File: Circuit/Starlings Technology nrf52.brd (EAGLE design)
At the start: 53.3 x 52.7 mm, 54 parts, among them IC1 MCP1703CB, J4 USB Micro, J7 CORTEX_DEBUG_SMD, Q2 BSS84, SW1 FSM8JSMASTR, SW2 FSM8JSMASTR, U1 TPS61259YFFR, U2 MCP73831, U3 BC840M, U5 74AHCT2G125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

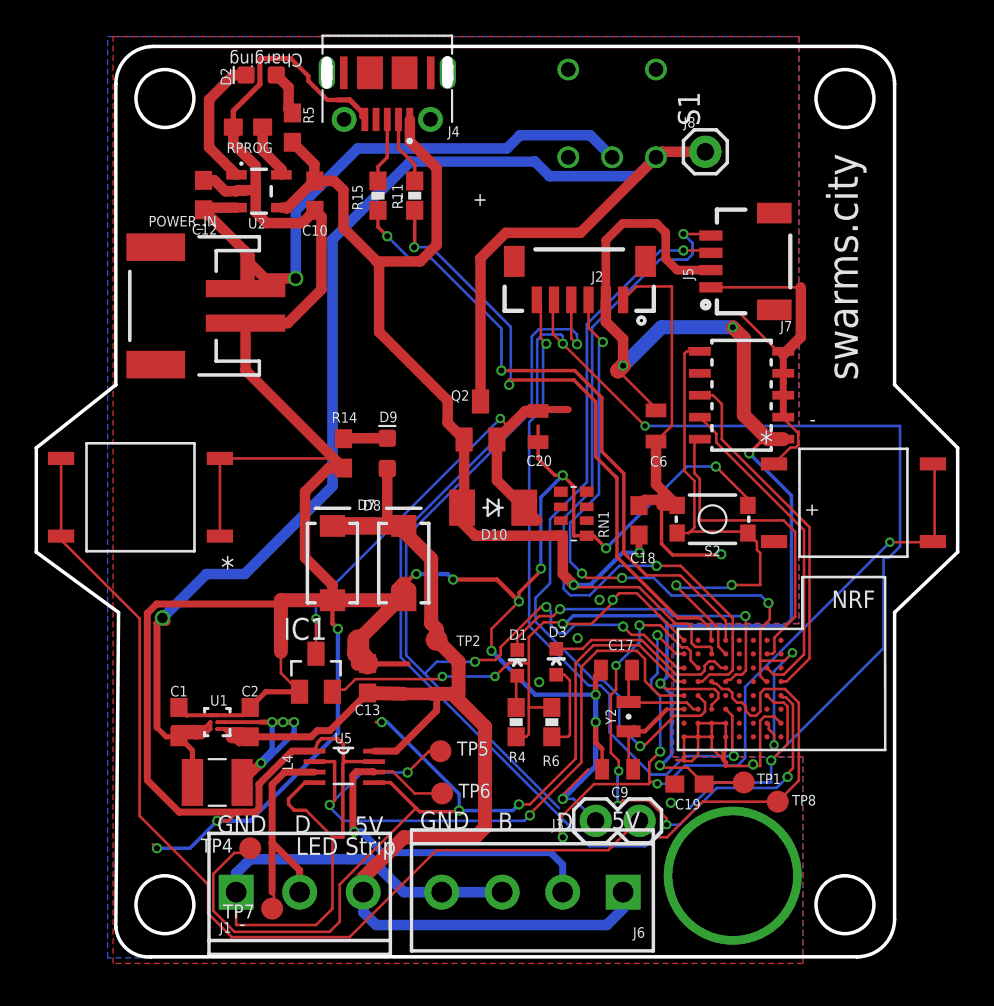
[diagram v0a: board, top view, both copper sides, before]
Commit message: Switching 3.5mm terminal blocks to 2.54mm (0.1") pitch header pins for painless led attachment. Also making buttons perfectly symmetric.
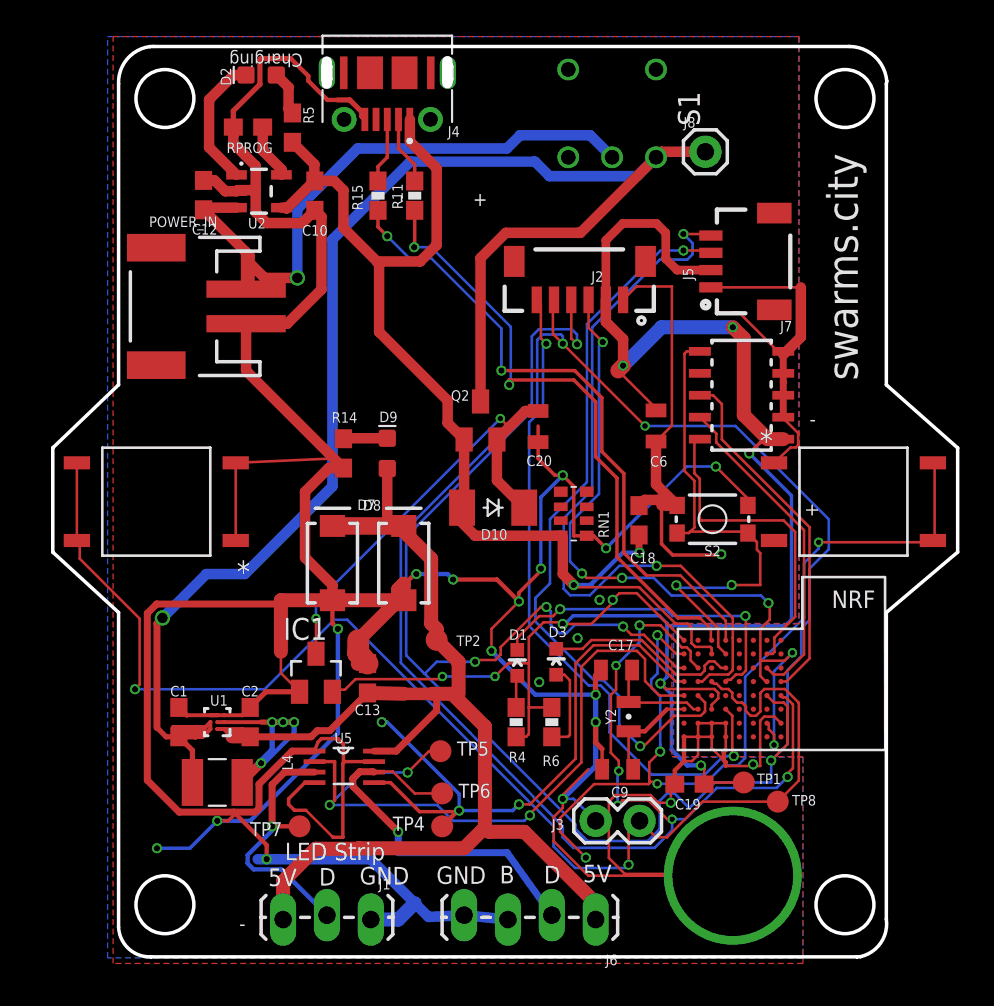
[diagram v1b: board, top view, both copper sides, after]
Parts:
- J1: device SparkFun-Connectors:SCREWTERMINAL-3.5MM-3_LOCK.007S -> SparkFun-Connectors:1X03_LOCK_LONGPADS
- J6: device SparkFun-Connectors:SCREWTERMINAL-3.5MM-4 -> SparkFun-Connectors:1X04_LOCK_LONGPADS
- moved TP4 11.2 mm to (14.9, 7.94)
- moved J1 7.78 mm to (10.8, 2.54), turned to 180 degrees
- moved TP7 5.02 mm to (6.67, 7.94)
- moved J6 2.25 mm to (23.8, 2.54)
- moved SW1 0.95 mm to (-1.63, 26.7)
- moved SW2 0.06 mm to (38.7, 26.7)
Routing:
- net HEADLAMP_3V3: track 56.5 -> 35.3 mm
- net GND: track 333.3 -> 352.4 mm, vias 21 -> 22
- net SWITCH_2: track 47.6 -> 51.8 mm
- net SWITCH_1: track 81.5 -> 77.8 mm, vias 0 -> 2
- net 5V: track 88.8 -> 85.6 mm
- net N$4: track 29.4 -> 26.4 mm
- net HEADLAMP_5V: track 13.6 -> 15.3 mm, vias 0 -> 1
- net PIN_03: track 113.8 -> 115.5 mm
- net STRIP_5V: track 23.6 -> 22.0 mm
- net 3.3V: track 112.3 -> 111.2 mm
- net VBAT: track 99.3 -> 98.3 mm
- net PIN_02: track 81.8 -> 82.8 mm
- net RESET: track 30.0 -> 29.3 mm
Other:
- board size 53.3 x 52.7 mm -> 52.4 x 52.7 mm

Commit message: Revision 11 of the board, with in stock and bigger boost converter and inductor.
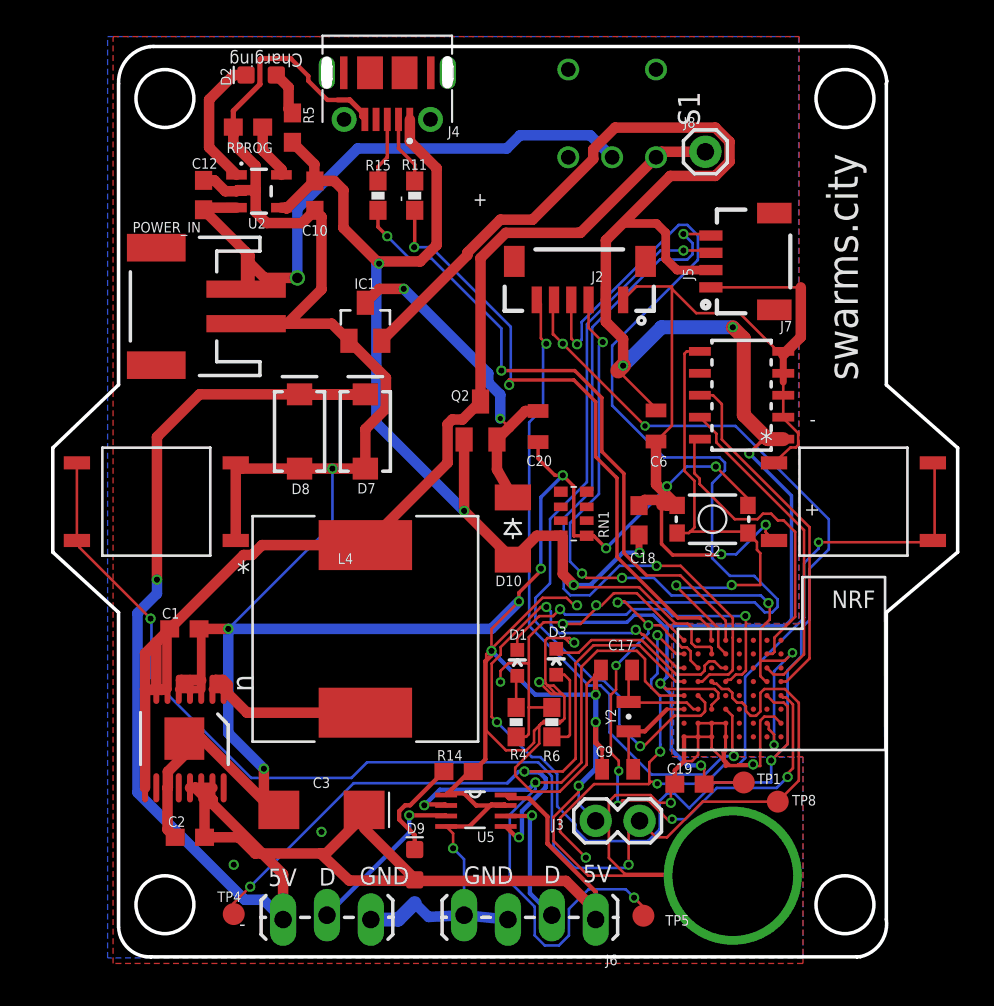
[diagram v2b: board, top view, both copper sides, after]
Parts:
- removed C13: 10uF, SparkFun-Capacitors:0603
- removed TP2, TP6, TP7: TPSB1,27, testpad:B1,27
- added C3: 220µF, SparkFun-Capacitors:EIA6032-NOM
- C2: value 10uF -> 2.2uF
- L4: device 1277AS-H-1R0M_P2:INDC3225X120N -> 12mm Inductor:IND_BOURNS_SRR1260
- U1: value TPS61259YFFR -> TPS61032PWP; device TPS6125x:YFF0009ACAG -> TPS61031PWPR:PWP0016K_N
- moved D9 23.9 mm to (13.3, 5.71)
- moved IC1 20.5 mm to (10.5, 37.1)
- moved R14 19.6 mm to (15.9, 11.1), turned to 0 degrees
- moved TP5 15.1 mm to (26.6, 2.76)
- moved TP4 13.1 mm to (2.86, 2.86)
- moved L4 12.3 mm to (10.5, 19.4), turned to 270 degrees
- moved U5 8.03 mm to (16.8, 8.89)
- moved D7 7.94 mm to (10.5, 30.8)
- moved D8 7.85 mm to (6.67, 30.8)
- moved C2 7.53 mm to (0.32, 7.30), turned to 180 degrees
- moved C1 5.41 mm to (0.00, 19.4), turned to 0 degrees
- moved U1 2.13 mm to (0.00, 13.0), turned to 270 degrees
- moved D10 1.66 mm to (19.0, 25.2), turned to 270 degrees
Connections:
- net 5V: now also C3.A, U1.13, U1.14, U1.15; no longer C13.1, TP2.TP, U1.A1, U1.A2
- net GND: now also C3.C, U1.11, U1.17, U1.3, U1.4, U1.5; no longer C13.2, U1.C1, U1.C2, U1.C3
- net HEADLAMP_5V: no longer TP7.TP
- net N$3: now also L4.2, U1.1, U1.2; no longer L4.1, U1.B1, U1.B2
- net STRIP_5V: no longer TP6.TP
- net VBAT: now also L4.1, U1.6, U1.7, U1.8, U1.9; no longer L4.2, U1.A3, U1.B3
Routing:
- net PIN_03: track 115.5 -> 85.4 mm
- net 5V: track 85.6 -> 114.0 mm, vias 0 -> 1
- net 3.3V: track 111.2 -> 137.8 mm, vias 9 -> 8
- net VBAT: track 98.3 -> 75.6 mm, vias 1 -> 0
- net STRIP_5V: track 22.0 -> 7.89 mm
- net GND: track 352.4 -> 365.7 mm, vias 22 -> 24
- net HEADLAMP_3V3: track 35.3 -> 43.5 mm
- net N$4: track 26.4 -> 19.8 mm
- net PIN_02: track 82.8 -> 88.9 mm, vias 7 -> 8
- net HEADLAMP_5V: track 15.3 -> 9.90 mm
- net VBUS: track 67.8 -> 71.6 mm, vias 2 -> 4
- net N$13: track 2.55 -> 6.13 mm
- net STRIP_3V3: track 41.6 -> 44.9 mm
- net N$3: track 14.1 -> 11.3 mm, vias 4 -> 0
- net SWITCH_1: track 77.8 -> 75.7 mm
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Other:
- board text added: "Swarm Lights V11 4/12/2022 starlings.technology"
- board text removed: "B"
- board text removed: "LED Strip"
- board text removed: "Swarm Lights V10 3/11/2022 starlings.technology"

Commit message: Switching to new tactile switches, separating external interfaces for easier reach and to get around enclosure ties.
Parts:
- removed J3: (no value), SparkFun-Connectors:1X02
- removed SW1, SW2: FSM8JSMASTR, FSM8JSMASTR:SW4_FSM8JSMASTR_TEC
- removed TP8: TPSB1,27, testpad:B1,27
- added S3, S4: TL1105, SparkFun-Switches:TACTILE_SWITCH_PTH_6.0MM
- moved TP4 12.4 mm to (15.2, 4.13)
- moved R5 10.2 mm to (16.4, 49.3)
- moved RPROG 9.85 mm to (13.5, 48.7)
- moved D2 9.26 mm to (13.7, 50.5)
- moved TP5 5.41 mm to (26.3, 8.16)
- moved J8 5.40 mm to (35.6, 47.0)
- moved S1 5.40 mm to (30.2, 49.2)
- moved J4 4.76 mm to (6.99, 51.2)
- moved J1 1.59 mm to (9.21, 2.54)
- moved J6 1.31 mm to (25.1, 2.86), turned to 0 degrees
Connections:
- net GND: now also S3.1, S4.1; no longer J3.1, SW1.1, SW1.2, SW2.1, SW2.2
- net SWITCH_1: now also S3.3; no longer J3.2, SW1.3, SW1.4, TP8.TP
- net SWITCH_2: now also S4.3; no longer SW2.3, SW2.4
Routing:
- net SWITCH_1: track 75.7 -> 12.3 mm, vias 2 -> 0
- net GND: track 365.7 -> 314.4 mm, vias 24 -> 23
- net 5V: track 114.0 -> 82.6 mm
- net STRIP_3V3: track 44.9 -> 28.4 mm, vias 3 -> 2
- net VBUS: track 71.6 -> 58.1 mm
- net 3.3V: track 137.8 -> 150.6 mm
- net HEADLAMP_3V3: track 43.5 -> 53.0 mm
- net N$14: track 7.74 -> 0.00 mm
- net STRIP_5V: track 7.89 -> 1.71 mm
- net VBAT: track 75.6 -> 81.0 mm
- net VBAT_RAW: track 37.8 -> 43.2 mm
- net SWITCH_2: track 51.8 -> 47.3 mm
- net N$16: track 3.79 -> 0.66 mm
- net N$12: track 3.95 -> 0.95 mm
- net N$11: track 3.21 -> 0.32 mm
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
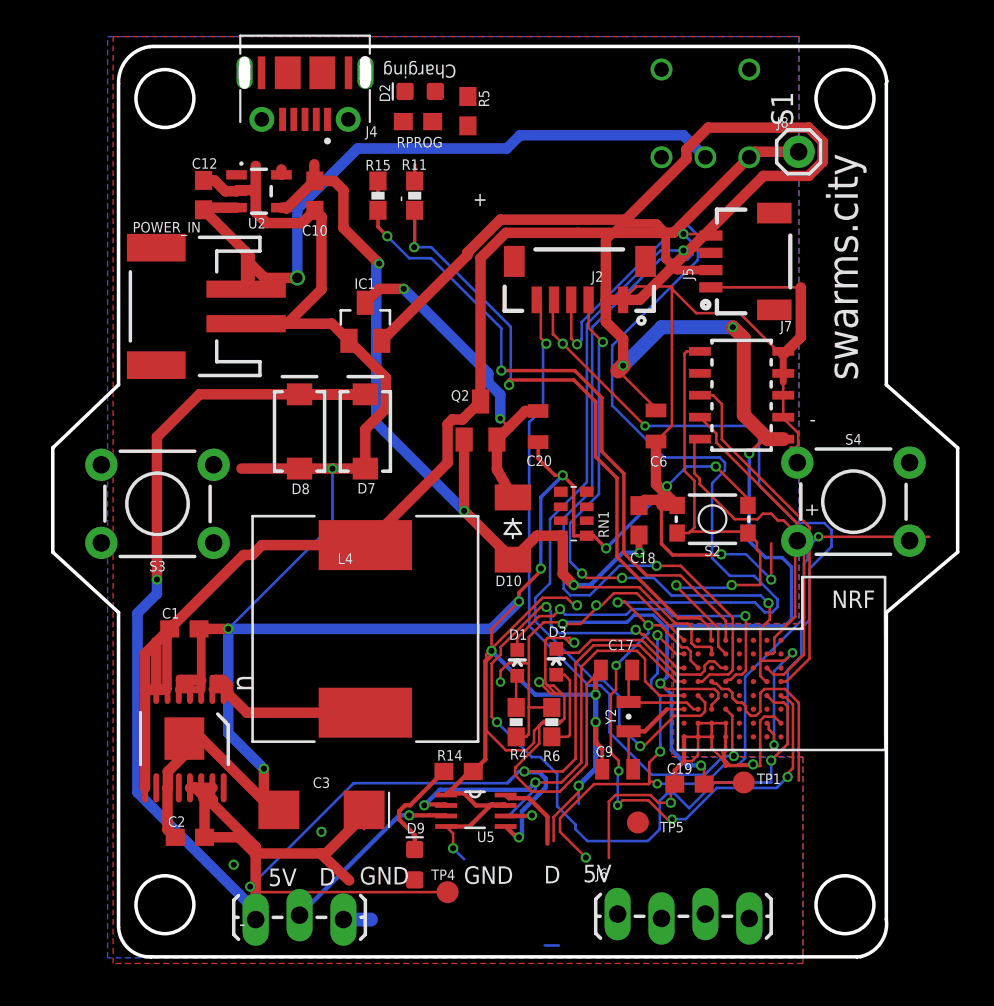
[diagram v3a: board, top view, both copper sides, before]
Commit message: Revision 12, changes out buttons and resistors.
- PTH tactile switches for taller buttons
- Resistor array and digikey swap
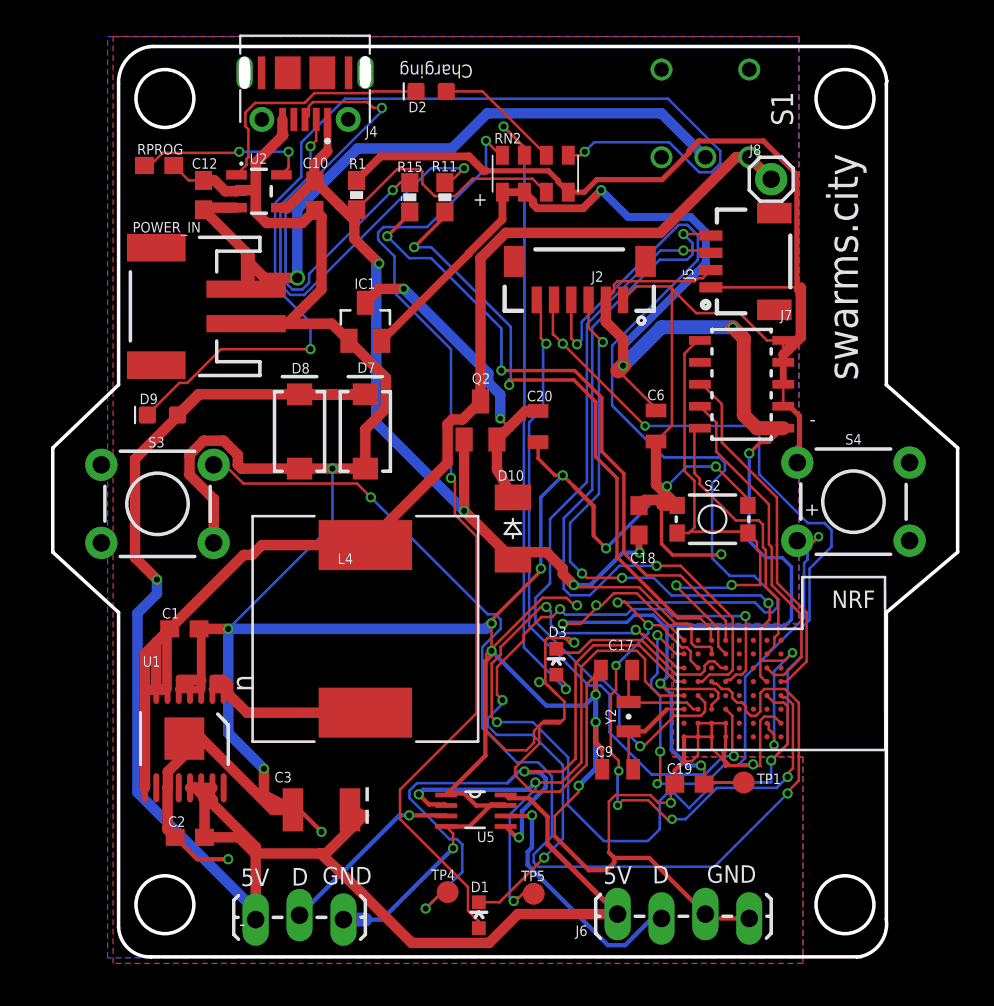
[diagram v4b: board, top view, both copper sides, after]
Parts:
- removed R14, R5: 1k, SparkFun-Resistors:0603
- removed R4, R6: 330, SparkFun:0603-RES
- removed RN1: 100K, resistor-dil:EXB38V
- added R1: 100k, SparkFun:0603-RES
- added RN2: (no value), resistor-dil:EXBS8V
- C3: value 220µF -> 220uF; device SparkFun-Capacitors:EIA6032-NOM -> SparkFun-Capacitors:EIA3528
- RPROG: value 2.0k -> 5.0k
- moved D9 29.9 mm to (-1.27, 31.8), turned to 180 degrees
- moved RPROG 15.2 mm to (-1.46, 46.2), turned to 0 degrees
- moved D1 14.8 mm to (17.0, 2.79)
- moved TP5 7.31 mm to (20.2, 4.03)
- moved J8 2.25 mm to (34.0, 45.4)
- moved R15 1.84 mm to (13.0, 44.4)
- moved R11 1.75 mm to (15.1, 44.4)
- moved D2 0.63 mm to (14.3, 50.5)
- moved J7 0.63 mm to (32.3, 33.5)
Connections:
- net 3.3V: now also RN2.1, RN2.2; no longer R4.1, R6.2
- net GND: now also R1.1, RN2.4; no longer R14.2, RN1.1
- net N$1: now also RN2.8; no longer R4.2
- net N$13: now also RN2.5; no longer R14.1
- net N$15: now also RN2.6; no longer R5.1
- net N$8: now also RN2.7; no longer R6.1
- net VBUS: now also R1.2, RN2.3; no longer R5.2, RN1.8
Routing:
- net GND: track 314.4 -> 382.3 mm, vias 23 -> 22
- net N$13: track 6.13 -> 61.8 mm, vias 0 -> 2
- net N$1: track 1.86 -> 57.1 mm, vias 0 -> 2
- net SWITCH_1: track 12.3 -> 67.5 mm, vias 0 -> 2
- net N$8: track 5.18 -> 37.3 mm, vias 0 -> 2
- net 3.3V: track 150.6 -> 119.6 mm
- net N$16: track 0.66 -> 28.0 mm, vias 0 -> 2
- net N$12: track 0.95 -> 25.8 mm, vias 0 -> 2
- net 5V: track 82.6 -> 107.3 mm
- net LED_1: track 19.6 -> 40.8 mm, vias 2 -> 4
- net VBUS: track 58.1 -> 73.4 mm
- net SWITCH_2: track 47.3 -> 32.8 mm, vias 5 -> 4
- net N$14: track 0.00 -> 14.3 mm
- net STRIP_5V: track 1.71 -> 14.8 mm
- net HEADLAMP_3V3: track 53.0 -> 40.8 mm
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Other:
- board text added: "Swarm Lights V12 4/28/2022 starlings.technology"
- board text removed: "Swarm Lights V11 4/12/2022 starlings.technology"
